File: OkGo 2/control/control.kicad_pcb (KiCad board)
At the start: 2 copper layers, 92.2 x 64.5 mm, 69 parts, among them M3_MOUNT VAL**, P102 KEYSW, P105 BATT, P106 ARM_LED, P108 SMA, P110 POWER_SW, P111 SERIAL, P201 CH1, P202 CH2, P205 CH3, P206 CH4, Q201 BSS138BK, Q202 BSS138BK, Q203 BSS138BK, Q204 BSS138BK, U101 SWD, U102 STM32F071CBT6, U103 MEJ2S0305SC, U105 RFM95W, U106 LCD_HD44780, U107 ADP3335, Y101 8MHz

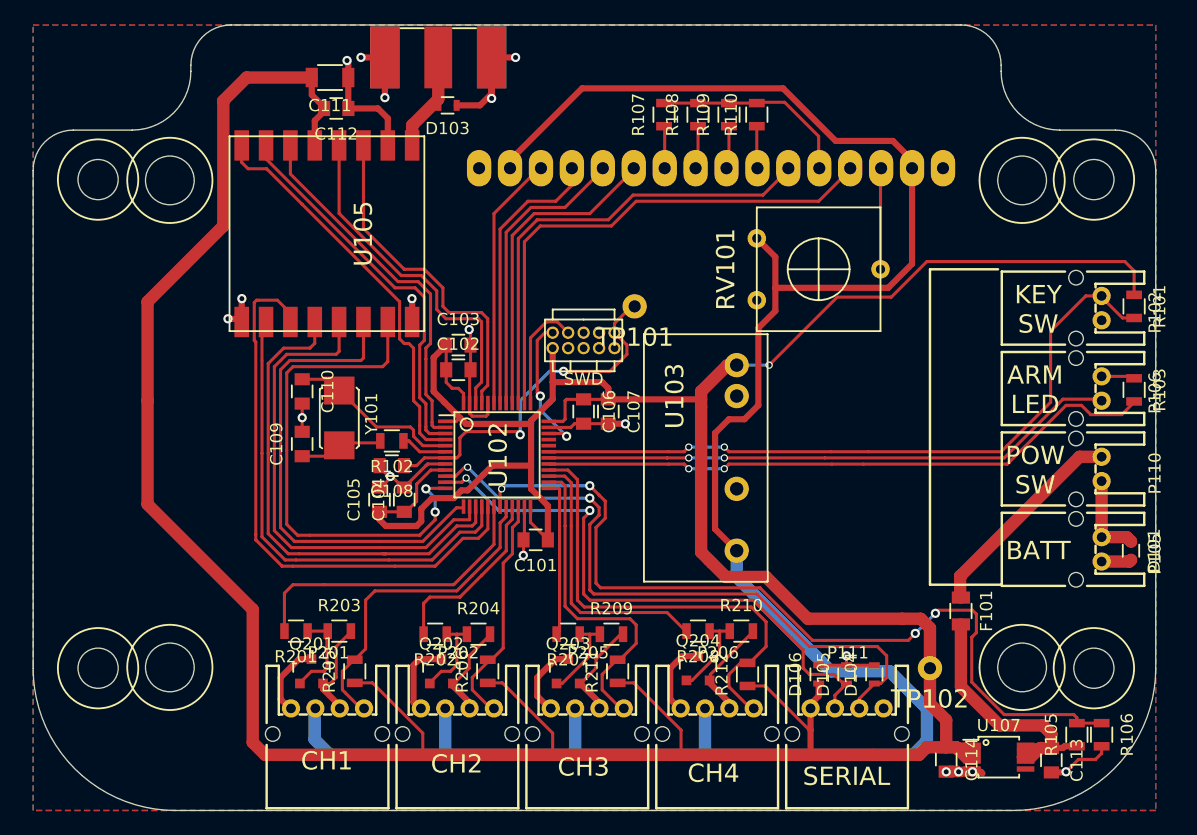
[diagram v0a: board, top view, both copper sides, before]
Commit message: Chunkied vias, rerouted some bits, resolves #36
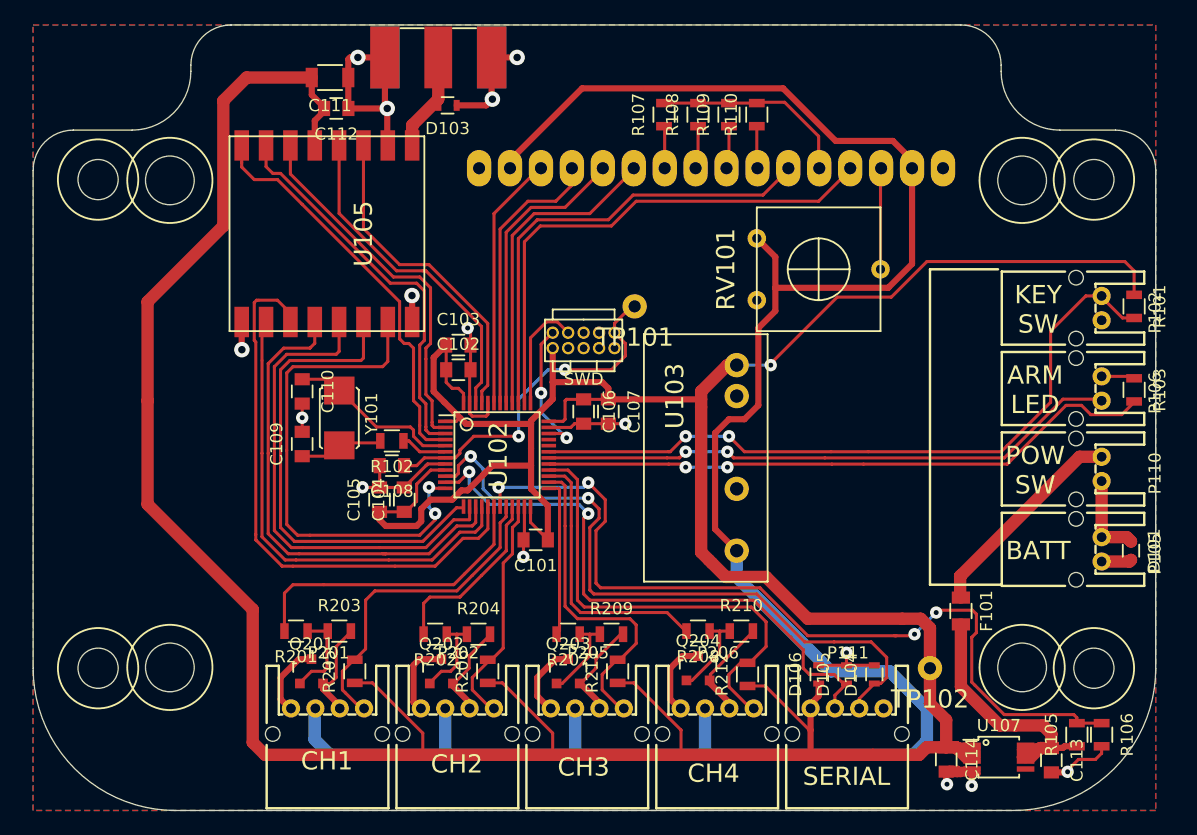
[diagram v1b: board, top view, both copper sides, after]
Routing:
- net GND: track 137.8 -> 140.7 mm, vias 18 -> 15
- net Net-(D104-Pad1): track 53.7 -> 55.5 mm
- net /RFM_DIO1: track 31.5 -> 33.0 mm
- net /RFM_DIO3: track 27.8 -> 26.7 mm
- net /RFM_DIO4: track 28.4 -> 27.3 mm
- net /nRST: track 29.9 -> 29.0 mm
- net /ARM_SW: track 58.4 -> 59.1 mm
- net Net-(D105-Pad1): track 48.3 -> 48.8 mm
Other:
- net class Default: clearance 0.2 -> 0.1778; trace_width 0.25 -> 0.254; via_dia 0.6 -> 1.016; via_drill 0.4 -> 0.4064
- rule trace_clearance: 0.2 -> 0.1778
- rule trace_min: 0.2 -> 0.2032
- rule via_min_drill: 0.3 -> 0.4064
- rule via_min_size: 0.4 -> 1.016

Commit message: Tidied control except cusf logo, partial #30
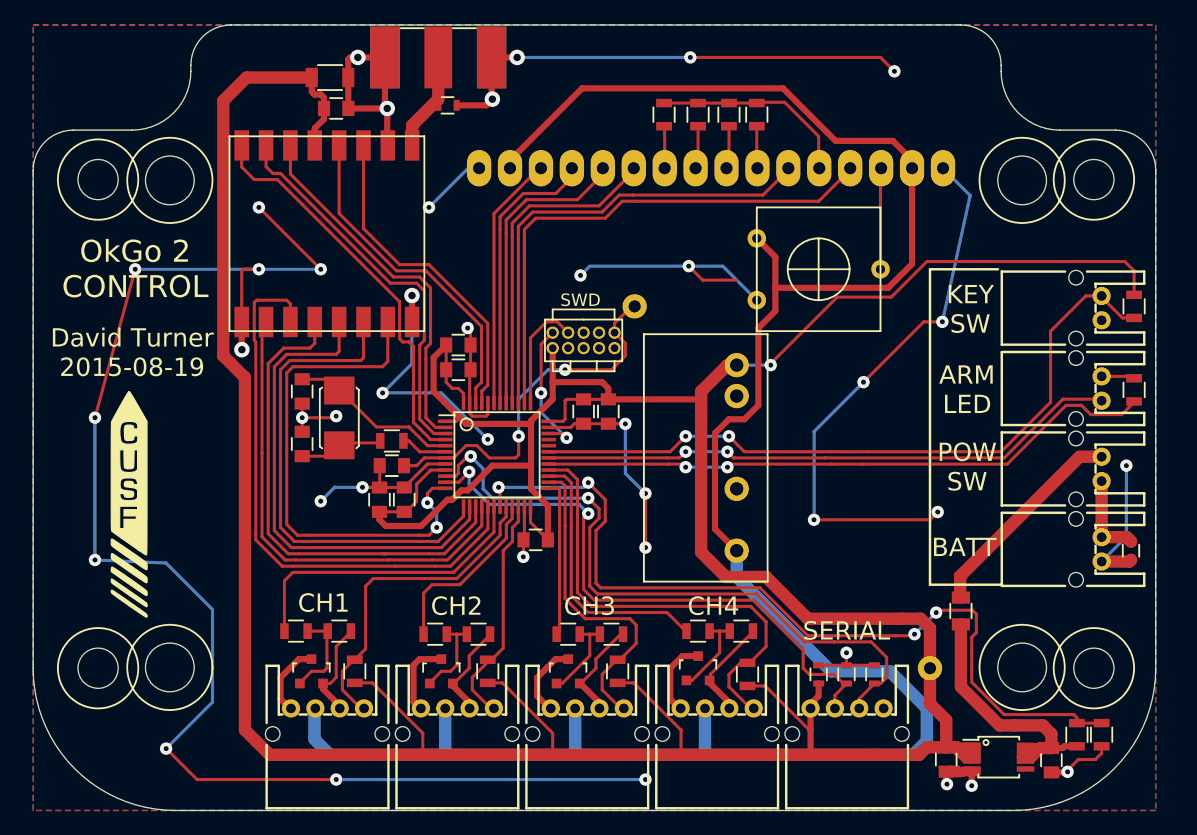
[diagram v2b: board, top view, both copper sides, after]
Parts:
- added G***: LOGO, control:wile-e-plunger, B.Cu at (149.4, 100.6)
- added G***: LOGO, common:cusf_logo, F.Cu at (140.5, 106.9)
- TP101: value nRST -> RESET
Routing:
- net GND: track 140.7 -> 406.1 mm, vias 15 -> 40
- net +3V3: track 352.1 -> 347.0 mm
- net /nRST: track 29.0 -> 30.6 mm
- net /LCD_DB5: track 24.1 -> 25.1 mm
- net /RFM_MOSI: track 46.5 -> 47.4 mm
- net /LCD_DB4: track 26.0 -> 26.9 mm
- net /LCD_RS: track 42.5 -> 43.1 mm
- net /LCD_E: track 38.0 -> 38.6 mm
- net /RFM_RESET: track 40.0 -> 40.5 mm
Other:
- board text added: "David Turner 2015-08-19"
- board text added: "OkGo 2 CONTROL"

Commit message: Control is photo-ready. Resolves #30
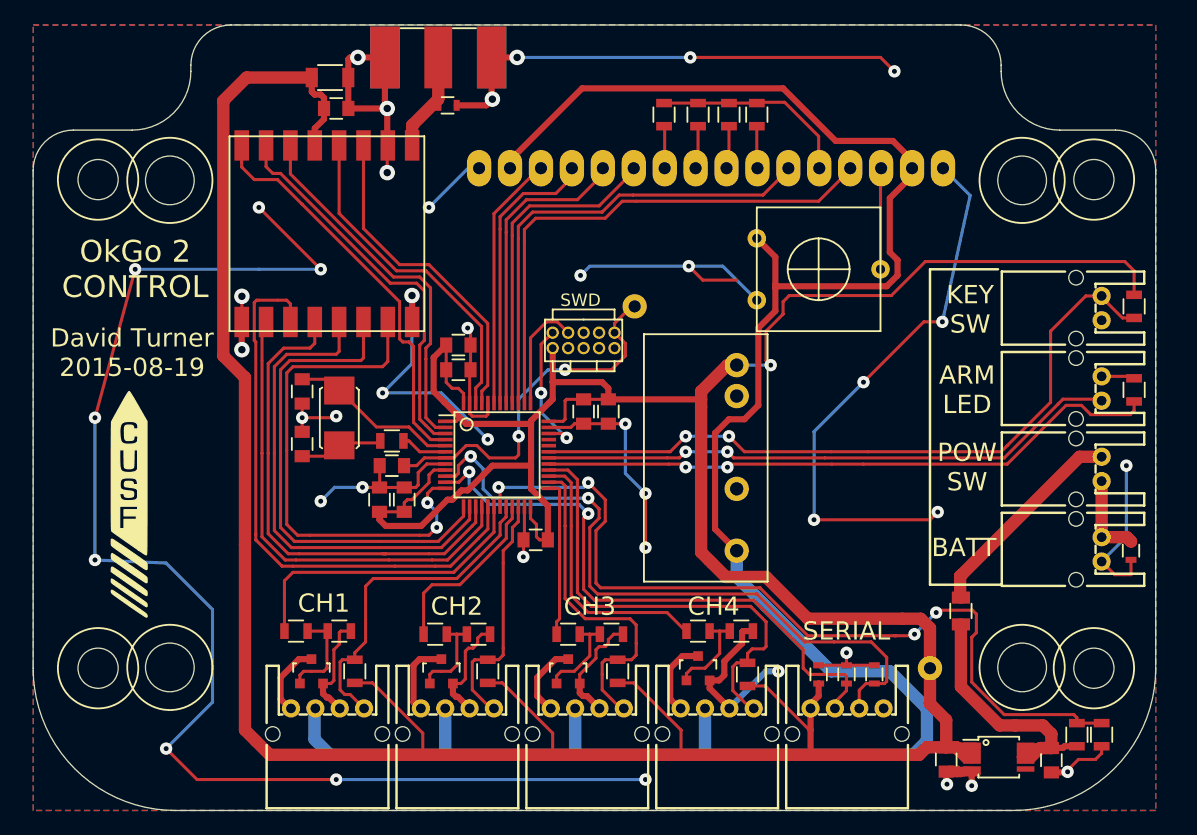
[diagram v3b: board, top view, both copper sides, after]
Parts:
- added G***: LOGO, common:cusf_logo_full, B.Cu at (201.0, 97.4)
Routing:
- net (no net): track 0.00 -> 111.4 mm, vias 0 -> 8
- net GND: track 406.1 -> 305.5 mm, vias 40 -> 34
- net +3V3: track 347.0 -> 350.5 mm
- net /controls/CH2_SW: track 19.3 -> 20.8 mm
- net /controls/CH3_SW: track 26.7 -> 27.8 mm
- net /controls/CH1_SW: track 27.2 -> 28.0 mm
- net Net-(D105-Pad1): track 48.6 -> 49.3 mm
- net Net-(D104-Pad1): track 55.3 -> 55.9 mm

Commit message: Fixed weird wayward ground stitching
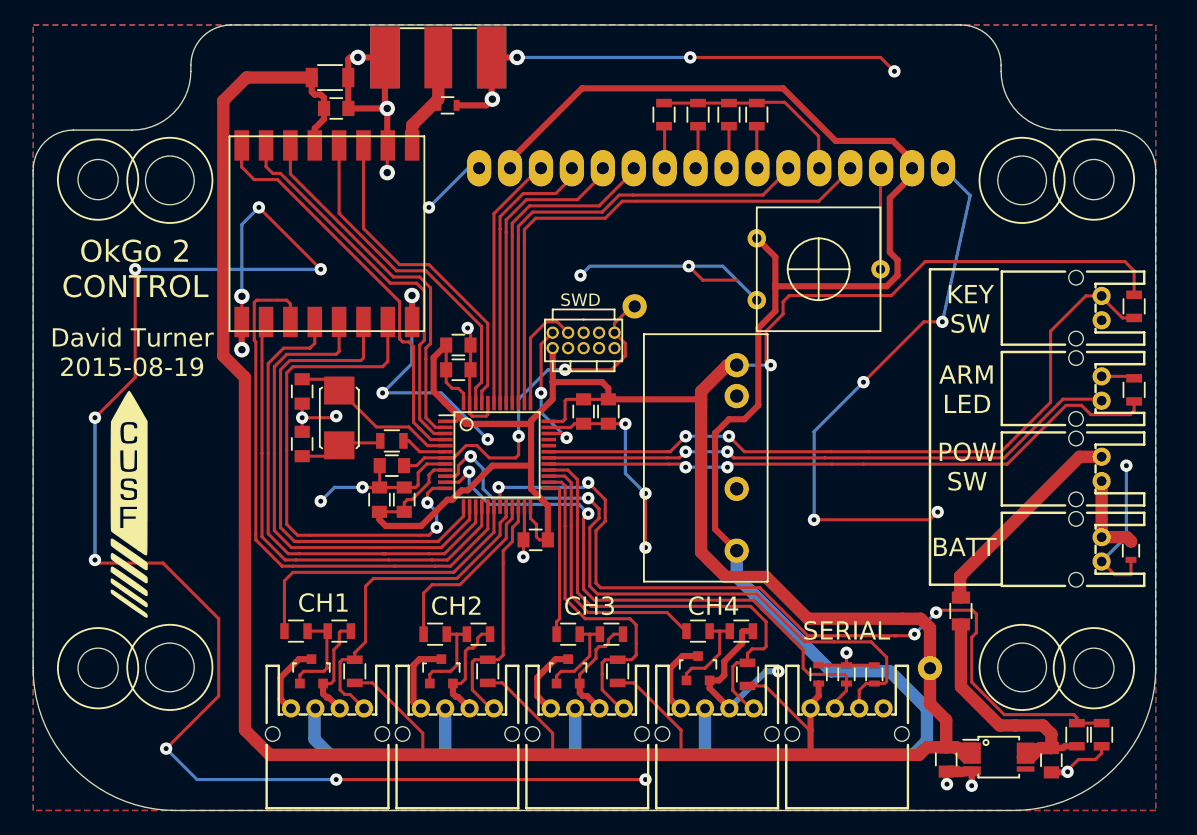
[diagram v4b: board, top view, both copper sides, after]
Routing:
- net GND: track 305.5 -> 426.1 mm, vias 34 -> 42
- net (no net): track 111.4 -> 0.00 mm, vias 8 -> 0
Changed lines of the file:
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@@
-(kicad_pcb (version 4) (host pcbnew 0.201508170901+6097~28~ubuntu14.04.1-product)
+(kicad_pcb (version 4) (host pcbnew 0.201508190901+6103~28~ubuntu14.04.1-product)
   (general
     (links 172)
@@
     (thickness 1.6)
     (drawings 30)
-    (tracks 1117)
+    (tracks 1120)
     (zones 0)
     (modules 72)
@@
   (gr_arc (start 216.916 71.374) (end 216.916 76.2) (angle 90) (layer Edge.Cuts) (width 0.1))
   (gr_arc (start 140.716 71.374) (end 145.542 71.374) (angle 90) (layer Edge.Cuts) (width 0.1))
-  (segment (start 137.668 111.506) (end 143.51 111.76) (width 0.254) (layer B.Cu) (net 0))
-  (segment (start 151.13 87.63) (end 140.97 87.63) (width 0.254) (layer B.Cu) (net 0))
-  (via (at 137.668 111.506) (size 1.016) (drill 0.4064) (layers F.Cu B.Cu) (net 0))
-  (segment (start 137.668 99.822) (end 137.668 111.506) (width 0.254) (layer B.Cu) (net 0))
-  (via (at 137.668 99.822) (size 1.016) (drill 0.4064) (layers F.Cu B.Cu) (net 0))
-  (segment (start 140.97 87.63) (end 137.668 99.822) (width 0.254) (layer F.Cu) (net 0))
-  (via (at 140.97 87.63) (size 1.016) (drill 0.4064) (layers F.Cu B.Cu) (net 0))
-  (via (at 182.88 129.54) (size 1.016) (drill 0.4064) (layers F.Cu B.Cu) (net 0))
-  (segment (start 157.48 129.54) (end 182.88 129.54) (width 0.254) (layer B.Cu) (net 0))
-  (via (at 157.48 129.54) (size 1.016) (drill 0.4064) (layers F.Cu B.Cu) (net 0))
-  (segment (start 146.05 129.54) (end 157.48 129.54) (width 0.254) (layer F.Cu) (net 0))
-  (segment (start 143.51 127) (end 146.05 129.54) (width 0.254) (layer F.Cu) (net 0))
-  (via (at 143.51 127) (size 1.016) (drill 0.4064) (layers F.Cu B.Cu) (net 0))
-  (segment (start 147.32 123.19) (end 143.51 127) (width 0.254) (layer B.Cu) (net 0))
-  (segment (start 147.32 115.57) (end 147.32 123.19) (width 0.254) (layer B.Cu) (net 0))
-  (segment (start 143.51 111.76) (end 147.32 115.57) (width 0.254) (layer B.Cu) (net 0))
-  (via (at 151.13 82.55) (size 1.016) (drill 0.4064) (layers F.Cu B.Cu) (net 0))
-  (segment (start 156.21 87.63) (end 151.13 82.55) (width 0.254) (layer F.Cu) (net 0))
-  (via (at 156.21 87.63) (size 1.016) (drill 0.4064) (layers F.Cu B.Cu) (net 0))
-  (segment (start 151.13 87.63) (end 156.21 87.63) (width 0.254) (layer B.Cu) (net 0))
   (segment (start 163.068 107.553) (end 163.068 106.807) (width 0.254) (layer F.Cu) (net 1))
   (segment (start 165.501 104.12) (end 166.438 104.12) (width 0.254) (layer F.Cu) (net 1))
@@
   (segment (start 166.338 100.12) (end 167.342 100.12) (width 0.254) (layer F.Cu) (net 1))
   (segment (start 167.342 100.12) (end 167.64 99.822) (width 0.254) (layer F.Cu) (net 1))
+  (segment (start 143.51 127) (end 146.05 129.54) (width 0.254) (layer B.Cu) (net 2))
+  (segment (start 140.97 96.52) (end 137.668 99.822) (width 0.254) (layer F.Cu) (net 2))
+  (via (at 137.668 99.822) (size 1.016) (drill 0.4064) (layers F.Cu B.Cu) (net 2))
+  (segment (start 137.668 99.822) (end 137.668 111.506) (width 0.254) (layer B.Cu) (net 2))
+  (via (at 137.668 111.506) (size 1.016) (drill 0.4064) (layers F.Cu B.Cu) (net 2))
+  (segment (start 137.668 111.506) (end 137.922 111.76) (width 0.254) (layer F.Cu) (net 2))
+  (segment (start 137.922 111.76) (end 143.256 111.76) (width 0.254) (layer F.Cu) (net 2))
+  (segment (start 143.256 111.76) (end 147.828 116.332) (width 0.254) (layer F.Cu) (net 2))
+  (segment (start 147.828 116.332) (end 147.828 122.682) (width 0.254) (layer F.Cu) (net 2))
+  (segment (start 147.828 122.682) (end 143.51 127) (width 0.254) (layer F.Cu) (net 2))
+  (via (at 143.51 127) (size 1.016) (drill 0.4064) (layers F.Cu B.Cu) (net 2))
+  (segment (start 149.733 89.8525) (end 149.733 83.947) (width 0.254) (layer B.Cu) (net 2))
+  (via (at 149.733 89.8525) (size 1.27) (drill 0.6096) (layers F.Cu B.Cu) (net 2))
+  (segment (start 149.733 91.694) (end 149.733 89.8525) (width 0.254) (layer F.Cu) (net 2))
+  (via (at 140.97 87.63) (size 1.016) (drill 0.4064) (layers F.Cu B.Cu) (net 2))
+  (segment (start 156.21 87.63) (end 140.97 87.63) (width 0.254) (layer B.Cu) (net 2))
+  (via (at 156.21 87.63) (size 1.016) (drill 0.4064) (layers F.Cu B.Cu) (net 2))
+  (segment (start 151.13 82.55) (end 156.21 87.63) (width 0.254) (layer F.Cu) (net 2))
+  (via (at 151.13 82.55) (size 1.016) (drill 0.4064) (layers F.Cu B.Cu) (net 2))
+  (segment (start 149.733 83.947) (end 151.13 82.55) (width 0.254) (layer B.Cu) (net 2))
+  (segment (start 140.97 87.63) (end 140.97 96.52) (width 0.254) (layer F.Cu) (net 2))
+  (via (at 182.88 129.54) (size 1.016) (drill 0.4064) (layers F.Cu B.Cu) (net 2))
+  (segment (start 157.48 129.54) (end 182.88 129.54) (width 0.254) (layer F.Cu) (net 2))
+  (via (at 157.48 129.54) (size 1.016) (drill 0.4064) (layers F.Cu B.Cu) (net 2))
+  (segment (start 146.05 129.54) (end 157.48 129.54) (width 0.254) (layer B.Cu) (net 2))
   (segment (start 163.068 105.553) (end 164.0045 105.553) (width 0.254) (layer F.Cu) (net 2))
   (segment (start 164.9215 103.62) (end 166.438 103.62) (width 0.254) (layer F.Cu) (net 2))
@@
   (via (at 161.671 79.6925) (size 1.27) (drill 0.6096) (layers F.Cu B.Cu) (net 2))
   (segment (start 149.718 91.709) (end 149.733 91.694) (width 0.254) (layer F.Cu) (net 2))
-  (segment (start 149.733 91.694) (end 149.733 89.8525) (width 0.254) (layer F.Cu) (net 2))
-  (via (at 149.733 89.8525) (size 1.27) (drill 0.6096) (layers F.Cu B.Cu) (net 2))
   (segment (start 222.758 111.494) (end 222.758 112.7125) (width 0.254) (layer F.Cu) (net 2))
   (segment (start 221.4245 112.7125) (end 220.345 111.633) (width 0.254) (layer F.Cu) (net 2))

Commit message: Updated control placement to make adam happy
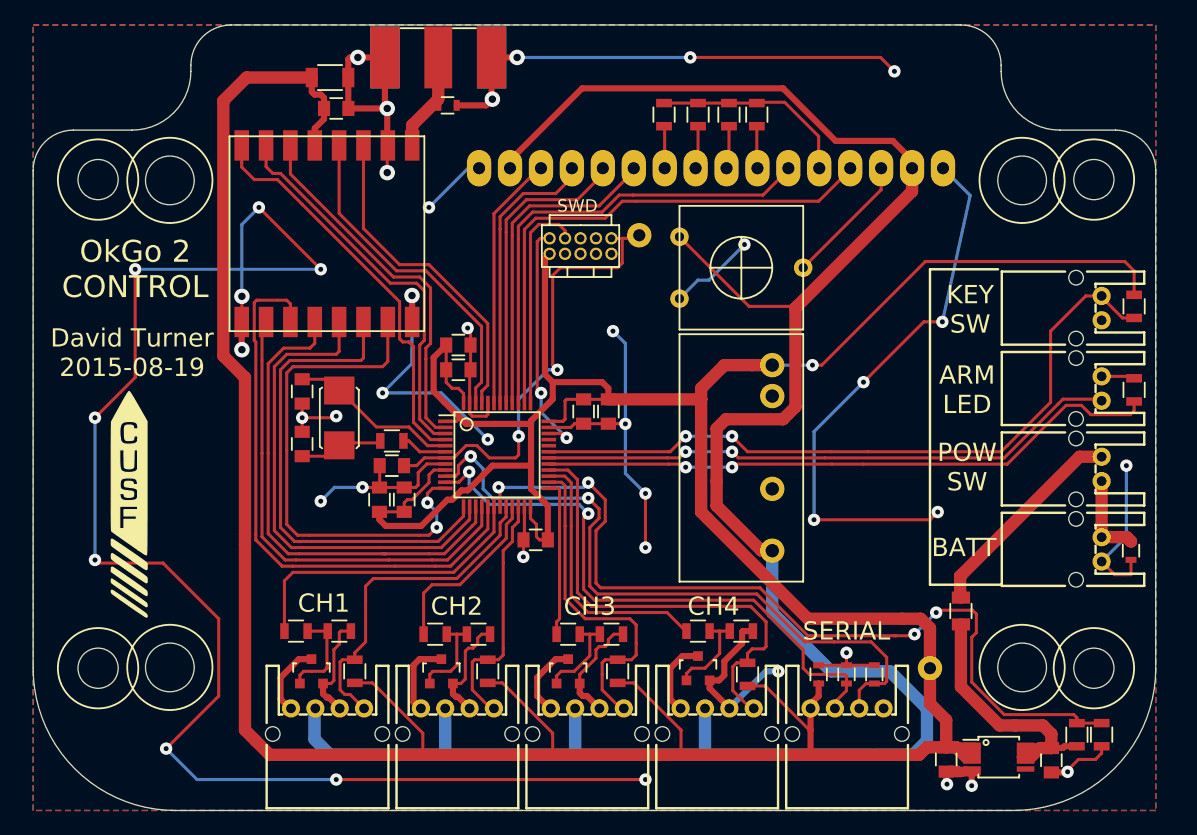
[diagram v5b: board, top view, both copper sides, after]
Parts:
- moved U101 7.75 mm to (175.0, 85.1)
- moved RV101 6.35 mm to (190.8, 87.5)
- moved TP101 5.85 mm to (182.4, 84.8)
- moved U103 2.92 mm to (193.3, 95.5)
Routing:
- net /SWDCLK: track 9.26 -> 17.9 mm
- net /SWDIO: track 11.5 -> 19.9 mm
- net /nRST: track 30.6 -> 37.7 mm
- net GND: track 426.1 -> 420.9 mm
- net +3V3: track 350.5 -> 354.5 mm
- net +5V: track 180.2 -> 184.2 mm
- net Net-(RV101-Pad2): track 8.31 -> 11.0 mm
